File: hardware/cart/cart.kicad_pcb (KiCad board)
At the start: 2 copper layers, 40.1 x 26.2 mm, 3 parts, among them J1 Front Edge, J2 Back Edge, U1 Pro Micro

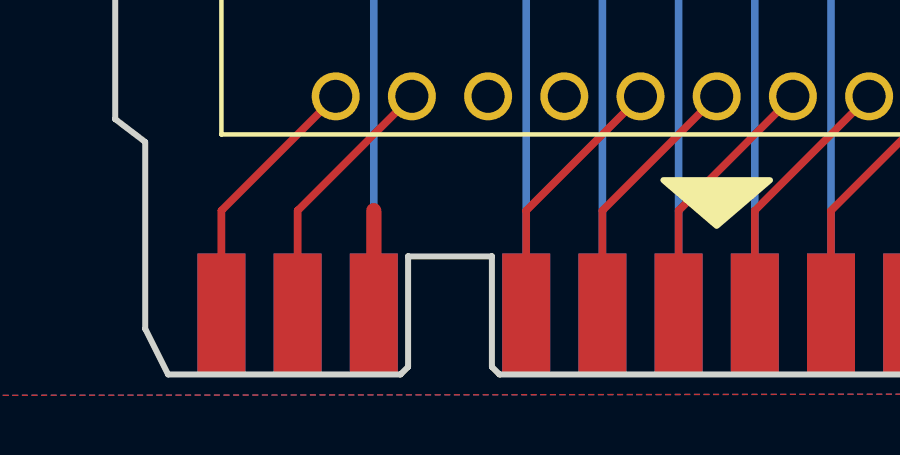
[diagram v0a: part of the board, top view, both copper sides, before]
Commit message: Add breakaway key pin filler
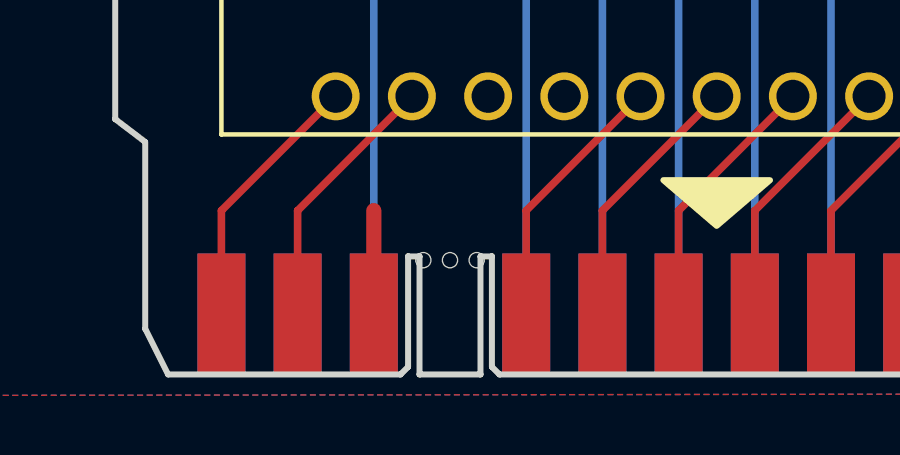
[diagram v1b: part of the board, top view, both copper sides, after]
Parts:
- added REF**: BREAKAWAY_HOLE, cart:BREAKAWAY_HOLE, F.Cu at (131.7, 124.8)
- added REF**: BREAKAWAY_HOLE, cart:BREAKAWAY_HOLE, F.Cu at (129.9, 124.8)
- added REF**: BREAKAWAY_HOLE, cart:BREAKAWAY_HOLE, F.Cu at (130.8, 124.8)
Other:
- outline, holes or cut-outs redrawn
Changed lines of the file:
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@@
   (general
     (thickness 1.6)
-    (drawings 41)
+    (drawings 45)
     (tracks 54)
     (zones 0)
-    (modules 3)
+    (modules 6)
     (nets 23)
   )
   (page USLetter)
   (layers
-    (0 F.Cu signal hide)
+    (0 F.Cu signal)
     (31 B.Cu signal hide)
     (32 B.Adhes user hide)
@@
     (36 B.SilkS user)
     (37 F.SilkS user)
-    (38 B.Mask user)
+    (38 B.Mask user hide)
     (39 F.Mask user hide)
     (40 Dwgs.User user hide)
@@
     (45 Margin user hide)
     (46 B.CrtYd user)
-    (47 F.CrtYd user hide)
+    (47 F.CrtYd user)
     (48 B.Fab user)
     (49 F.Fab user hide)
@@
     (mod_text_size 1 1)
     (mod_text_width 0.15)
-    (pad_size 5.15 5.15)
-    (pad_drill 0)
+    (pad_size 0.508 0.508)
+    (pad_drill 0.508)
     (pad_to_mask_clearance 0.0508)
     (solder_mask_min_width 0.25)
@@
     (add_net "Net-(J2-Pad8)")
     (add_net "Net-(J2-Pad9)")
+  )
+  (module cart:BREAKAWAY_HOLE (layer F.Cu)
+    (at 131.699 124.841)
+    (fp_text reference REF** (at 0 2.54) (layer F.SilkS) hide
+      (effects (font (size 1 1) (thickness 0.15)))
+    )
+    (fp_text value BREAKAWAY_HOLE (at 0 -2.54) (layer F.Fab)
+      (effects (font (size 1 1) (thickness 0.15)))
+    )
+    (pad "" np_thru_hole circle (at 0 0) (size 0.508 0.508) (drill 0.508) (layers *.Cu *.Mask))
+  )
+  (module cart:BREAKAWAY_HOLE (layer F.Cu)
+    (at 129.921 124.841)
+    (fp_text reference REF** (at 0 2.54) (layer F.SilkS) hide
+      (effects (font (size 1 1) (thickness 0.15)))
+    )
+    (fp_text value BREAKAWAY_HOLE (at 0 -2.54) (layer F.Fab)
+      (effects (font (size 1 1) (thickness 0.15)))
+    )
+    (pad "" np_thru_hole circle (at 0 0) (size 0.508 0.508) (drill 0.508) (layers *.Cu *.Mask))
+  )
+  (module cart:BREAKAWAY_HOLE (layer F.Cu)
+    (at 130.81 124.841)
+    (fp_text reference REF** (at 0 2.54) (layer F.SilkS) hide
+      (effects (font (size 1 1) (thickness 0.15)))
+    )
+    (fp_text value BREAKAWAY_HOLE (at 0 -2.54) (layer F.Fab)
+      (effects (font (size 1 1) (thickness 0.15)))
+    )
+    (pad "" np_thru_hole circle (at 0 0) (size 0.508 0.508) (drill 0.508) (layers *.Cu *.Mask))
   )
   (module cart:CARD_CONNECTOR_14_POS (layer B.Cu)
@@
       (net 3 "Net-(J1-Pad1)"))
   )
+  (gr_line (start 131.826 124.714) (end 132.207 124.714) (layer Edge.Cuts) (width 0.2))
+  (gr_line (start 129.794 128.651) (end 131.826 128.651) (layer Edge.Cuts) (width 0.2))
+  (gr_line (start 131.826 124.714) (end 131.826 128.651) (layer Edge.Cuts) (width 0.2))
+  (gr_line (start 129.794 124.714) (end 129.794 128.651) (layer Edge.Cuts) (width 0.2))
   (gr_text github.com/menehune23/arduboy-ce (at 139.7 122.301) (layer B.SilkS)
     (effects (font (size 0.762 0.762) (thickness 0.127)) (justify mirror))
@@
   (gr_line (start 132.461 128.651) (end 132.207 128.397) (layer Edge.Cuts) (width 0.2))
   (gr_line (start 129.413 128.397) (end 129.159 128.651) (layer Edge.Cuts) (width 0.2))
-  (gr_line (start 129.413 124.714) (end 132.207 124.714) (layer Edge.Cuts) (width 0.2))
+  (gr_line (start 129.413 124.714) (end 129.794 124.714) (layer Edge.Cuts) (width 0.2))
   (gr_line (start 132.207 124.714) (end 132.207 128.397) (layer Edge.Cuts) (width 0.2))
   (gr_line (start 129.413 124.714) (end 129.413 128.397) (layer Edge.Cuts) (width 0.2))

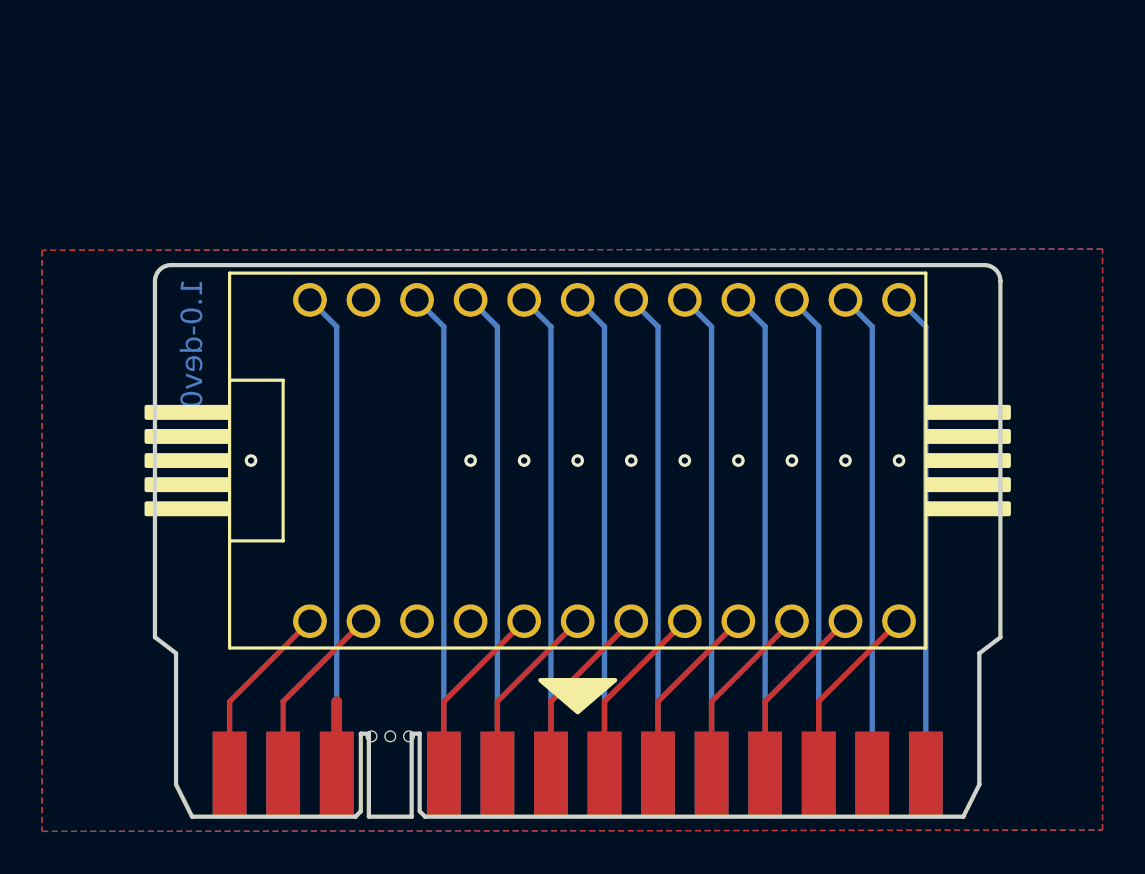
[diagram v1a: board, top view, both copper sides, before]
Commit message: System front/back, extend cart height
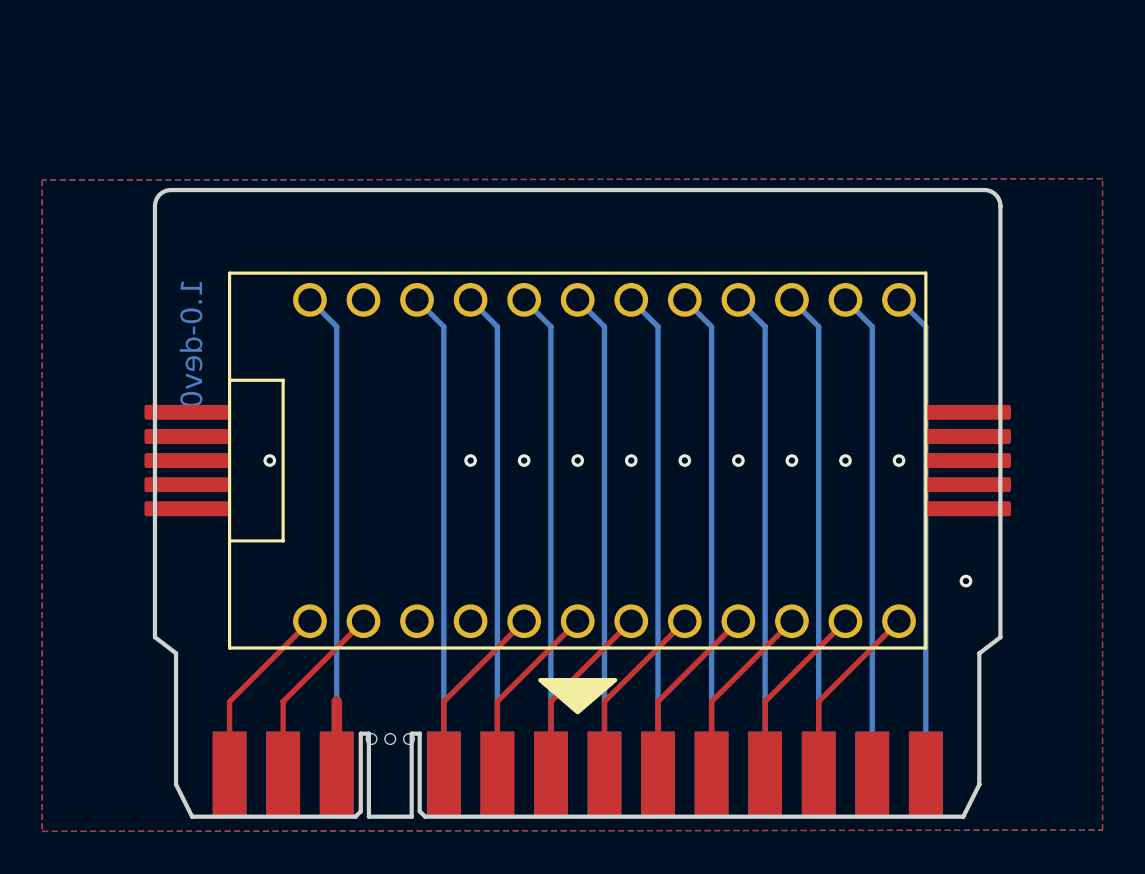
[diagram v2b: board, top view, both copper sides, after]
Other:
- board size 40.1 x 26.2 mm -> 40.1 x 29.7 mm
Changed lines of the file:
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@@
-(kicad_pcb (version 20171130) (host pcbnew "(5.1.2-1)-1")
+(kicad_pcb (version 20171130) (host pcbnew "(5.1.9-0-10_14)")
   (general
     (thickness 1.6)
-    (drawings 45)
+    (drawings 55)
     (tracks 54)
     (zones 0)
@@
   (layers
     (0 F.Cu signal)
-    (31 B.Cu signal hide)
+    (31 B.Cu signal)
     (32 B.Adhes user hide)
     (33 F.Adhes user hide)
@@
     (37 F.SilkS user)
     (38 B.Mask user hide)
-    (39 F.Mask user hide)
+    (39 F.Mask user)
     (40 Dwgs.User user hide)
     (41 Cmts.User user hide)
@@
       (effects (font (size 1 1) (thickness 0.15)))
     )
-    (pad "" np_thru_hole circle (at 0 0) (size 0.508 0.508) (drill 0.508) (layers *.Cu *.Mask))
+    (pad "" np_thru_hole circle (at 0 0.127) (size 0.508 0.508) (drill 0.508) (layers *.Cu *.Mask))
   )
   (module cart:BREAKAWAY_HOLE (layer F.Cu)
@@
       (effects (font (size 1 1) (thickness 0.15)))
     )
-    (pad "" np_thru_hole circle (at 0 0) (size 0.508 0.508) (drill 0.508) (layers *.Cu *.Mask))
+    (pad "" np_thru_hole circle (at 0 0.127) (size 0.508 0.508) (drill 0.508) (layers *.Cu *.Mask))
   )
   (module cart:BREAKAWAY_HOLE (layer F.Cu)
@@
       (effects (font (size 1 1) (thickness 0.15)))
     )
-    (pad "" np_thru_hole circle (at 0 0) (size 0.508 0.508) (drill 0.508) (layers *.Cu *.Mask))
+    (pad "" np_thru_hole circle (at 0 0.127) (size 0.508 0.508) (drill 0.508) (layers *.Cu *.Mask))
   )
   (module cart:CARD_CONNECTOR_14_POS (layer B.Cu)
@@
       (net 3 "Net-(J1-Pad1)"))
   )
+  (gr_poly (pts (xy 119.253 113.792) (xy 123.1265 113.792) (xy 123.1265 114.3) (xy 119.253 114.3)) (layer F.Cu) (width 0.2))
+  (gr_poly (pts (xy 119.253 112.649) (xy 123.1265 112.649) (xy 123.1265 113.157) (xy 119.253 113.157)) (layer F.Cu) (width 0.2))
+  (gr_poly (pts (xy 119.253 111.506) (xy 123.1265 111.506) (xy 123.1265 112.014) (xy 119.253 112.014)) (layer F.Cu) (width 0.2))
+  (gr_poly (pts (xy 119.253 110.363) (xy 123.1265 110.363) (xy 123.1265 110.871) (xy 119.253 110.871)) (layer F.Cu) (width 0.2))
+  (gr_poly (pts (xy 119.253 109.22) (xy 123.1265 109.22) (xy 123.1265 109.728) (xy 119.253 109.728)) (layer F.Cu) (width 0.2))
+  (gr_poly (pts (xy 156.2735 113.792) (xy 160.147 113.792) (xy 160.147 114.3) (xy 156.2735 114.3)) (layer F.Mask) (width 0.2))
+  (gr_poly (pts (xy 156.2735 112.649) (xy 160.147 112.649) (xy 160.147 113.157) (xy 156.2735 113.157)) (layer F.Mask) (width 0.2))
+  (gr_poly (pts (xy 156.2735 111.506) (xy 160.147 111.506) (xy 160.147 112.014) (xy 156.2735 112.014)) (layer F.Mask) (width 0.2))
+  (gr_poly (pts (xy 156.2735 110.363) (xy 160.147 110.363) (xy 160.147 110.871) (xy 156.2735 110.871)) (layer F.Mask) (width 0.2))
+  (gr_poly (pts (xy 156.2735 109.22) (xy 160.147 109.22) (xy 160.147 109.728) (xy 156.2735 109.728)) (layer F.Mask) (width 0.2))
   (gr_line (start 131.826 124.714) (end 132.207 124.714) (layer Edge.Cuts) (width 0.2))
   (gr_line (start 129.794 128.651) (end 131.826 128.651) (layer Edge.Cuts) (width 0.2))
@@
   (gr_line (start 129.413 124.714) (end 129.413 128.397) (layer Edge.Cuts) (width 0.2))
   (gr_line (start 157.988 128.651) (end 132.461 128.651) (layer Edge.Cuts) (width 0.2))
-  (gr_poly (pts (xy 119.253 113.792) (xy 123.1265 113.792) (xy 123.1265 114.3) (xy 119.253 114.3)) (layer F.SilkS) (width 0.2))
-  (gr_poly (pts (xy 119.253 110.363) (xy 123.1265 110.363) (xy 123.1265 110.871) (xy 119.253 110.871)) (layer F.SilkS) (width 0.2))
-  (gr_poly (pts (xy 119.253 112.649) (xy 123.1265 112.649) (xy 123.1265 113.157) (xy 119.253 113.157)) (layer F.SilkS) (width 0.2))
-  (gr_poly (pts (xy 119.253 111.506) (xy 123.1265 111.506) (xy 123.1265 112.014) (xy 119.253 112.014)) (layer F.SilkS) (width 0.2))
-  (gr_poly (pts (xy 119.253 109.22) (xy 123.1265 109.22) (xy 123.1265 109.728) (xy 119.253 109.728)) (layer F.SilkS) (width 0.2))
-  (gr_poly (pts (xy 156.2735 113.792) (xy 160.147 113.792) (xy 160.147 114.3) (xy 156.2735 114.3)) (layer F.SilkS) (width 0.2))
-  (gr_poly (pts (xy 156.2735 112.649) (xy 160.147 112.649) (xy 160.147 113.157) (xy 156.2735 113.157)) (layer F.SilkS) (width 0.2))
-  (gr_poly (pts (xy 156.2735 109.22) (xy 160.147 109.22) (xy 160.147 109.728) (xy 156.2735 109.728)) (layer F.SilkS) (width 0.2))
-  (gr_poly (pts (xy 156.2735 110.363) (xy 160.147 110.363) (xy 160.147 110.871) (xy 156.2735 110.871)) (layer F.SilkS) (width 0.2))
-  (gr_line (start 119.65 103.251) (end 119.65 120.139) (layer Edge.Cuts) (width 0.2))
+  (gr_poly (pts (xy 119.253 113.792) (xy 123.1265 113.792) (xy 123.1265 114.3) (xy 119.253 114.3)) (layer F.Mask) (width 0.2))
+  (gr_poly (pts (xy 119.253 110.363) (xy 123.1265 110.363) (xy 123.1265 110.871) (xy 119.253 110.871)) (layer F.Mask) (width 0.2))
+  (gr_poly (pts (xy 119.253 112.649) (xy 123.1265 112.649) (xy 123.1265 113.157) (xy 119.253 113.157)) (layer F.Mask) (width 0.2))
+  (gr_poly (pts (xy 119.253 111.506) (xy 123.1265 111.506) (xy 123.1265 112.014) (xy 119.253 112.014)) (layer F.Mask) (width 0.2))
+  (gr_poly (pts (xy 119.253 109.22) (xy 123.1265 109.22) (xy 123.1265 109.728) (xy 119.253 109.728)) (layer F.Mask) (width 0.2))
+  (gr_poly (pts (xy 156.2735 113.792) (xy 160.147 113.792) (xy 160.147 114.3) (xy 156.2735 114.3)) (layer F.Cu) (width 0.2))
+  (gr_poly (pts (xy 156.2735 112.649) (xy 160.147 112.649) (xy 160.147 113.157) (xy 156.2735 113.157)) (layer F.Cu) (width 0.2))
+  (gr_poly (pts (xy 156.2735 109.22) (xy 160.147 109.22) (xy 160.147 109.728) (xy 156.2735 109.728)) (layer F.Cu) (width 0.2))
+  (gr_poly (pts (xy 156.2735 110.363) (xy 160.147 110.363) (xy 160.147 110.871) (xy 156.2735 110.871)) (layer F.Cu) (width 0.2))
+  (gr_line (start 119.65 99.691) (end 119.65 120.139) (layer Edge.Cuts) (width 0.2))
   (gr_line (start 120.65 120.901) (end 119.65 120.139) (layer Edge.Cuts) (width 0.2))
-  (gr_arc (start 120.412 103.251) (end 120.412 102.489) (angle -90) (layer Edge.Cuts) (width 0.2))
+  (gr_arc (start 120.412 99.691) (end 120.412 98.929) (angle -90) (layer Edge.Cuts) (width 0.2))
   (gr_line (start 158.115 122.174) (end 158.115 105.283) (layer Dwgs.User) (width 0.15))
   (gr_line (start 159.75 120.142) (end 158.75 120.904) (layer Edge.Cuts) (width 0.2))
@@
   (gr_circle (center 174.625 93.98) (end 177.421885 93.98) (layer Cmts.User) (width 0.15))
   (gr_circle (center 174.625 88.265) (end 177.421885 88.265) (layer Cmts.User) (width 0.15))
-  (gr_poly (pts (xy 156.2735 111.506) (xy 160.147 111.506) (xy 160.147 112.014) (xy 156.2735 112.014)) (layer F.SilkS) (width 0.2))
-  (gr_line (start 159.75 103.251) (end 159.75 120.142) (layer Edge.Cuts) (width 0.2))
+  (gr_poly (pts (xy 156.2735 111.506) (xy 160.147 111.506) (xy 160.147 112.014) (xy 156.2735 112.014)) (layer F.Cu) (width 0.2))
+  (gr_line (start 159.75 99.691) (end 159.75 120.142) (layer Edge.Cuts) (width 0.2))
   (gr_poly (pts (xy 160.4645 124.6505) (xy 160.401 129.667) (xy 118.618 129.667) (xy 118.6815 124.6505)) (layer B.Mask) (width 0.1))
   (gr_poly (pts (xy 160.401 124.6505) (xy 160.401 129.667) (xy 118.618 129.667) (xy 118.618 124.6505)) (layer F.Mask) (width 0.1))
-  (gr_line (start 120.412 102.489) (end 158.988 102.489) (layer Edge.Cuts) (width 0.2))
-  (gr_arc (start 158.988 103.251) (end 159.75 103.251) (angle -90) (layer Edge.Cuts) (width 0.2))
+  (gr_line (start 120.412 98.929) (end 158.988 98.929) (layer Edge.Cuts) (width 0.2))
+  (gr_arc (start 158.988 99.691) (end 159.75 99.691) (angle -90) (layer Edge.Cuts) (width 0.2))
   (gr_text 1.0-dev0 (at 121.412 103.124 90) (layer B.Cu)
     (effects (font (size 1.016 1.016) (thickness 0.2286)) (justify left mirror))
@@
   (via (at 152.4 111.76) (size 0.6) (drill 0.3) (layers F.Cu B.Cu) (net 1))
   (via (at 154.94 111.76) (size 0.6) (drill 0.3) (layers F.Cu B.Cu) (net 1))
-  (via (at 158.115 111.76) (size 0.6) (drill 0.3) (layers F.Cu B.Cu) (net 1))
-  (via (at 124.206 111.76) (size 0.6) (drill 0.3) (layers F.Cu B.Cu) (net 1))
+  (via (at 158.115 117.475) (size 0.6) (drill 0.3) (layers F.Cu B.Cu) (net 1))
+  (via (at 125.095 111.76) (size 0.6) (drill 0.3) (layers F.Cu B.Cu) (net 1))
   (segment (start 125.73 123.19) (end 125.73 126.619) (width 0.254) (layer F.Cu) (net 2))
   (segment (start 129.54 119.38) (end 125.73 123.19) (width 0.254) (layer F.Cu) (net 2))
@@
     (polygon
       (pts
-        (xy 164.592 101.727) (xy 114.3 101.7905) (xy 114.3 129.3495) (xy 164.592 129.286)
+        (xy 164.592 98.39325) (xy 114.3 98.45675) (xy 114.3 129.3495) (xy 164.592 129.286)
       )
     )
@@
     (polygon
       (pts
-        (xy 164.592 101.727) (xy 114.3 101.7905) (xy 114.3 129.3495) (xy 164.592 129.286)
+        (xy 164.592 98.39325) (xy 114.3 98.45675) (xy 114.3 129.3495) (xy 164.592 129.286)
       )
     )

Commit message: Add JLC order number lables
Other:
- board text added: "JLCJLCJLCJLC"
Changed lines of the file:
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@@
   (general
     (thickness 1.6)
-    (drawings 55)
+    (drawings 56)
     (tracks 54)
     (zones 0)
@@
   (page USLetter)
   (layers
-    (0 F.Cu signal)
+    (0 F.Cu signal hide)
     (31 B.Cu signal)
     (32 B.Adhes user hide)
@@
     (35 F.Paste user hide)
     (36 B.SilkS user)
-    (37 F.SilkS user)
-    (38 B.Mask user hide)
-    (39 F.Mask user)
+    (37 F.SilkS user hide)
+    (38 B.Mask user)
+    (39 F.Mask user hide)
     (40 Dwgs.User user hide)
     (41 Cmts.User user hide)
@@
     (45 Margin user hide)
     (46 B.CrtYd user)
-    (47 F.CrtYd user)
+    (47 F.CrtYd user hide)
     (48 B.Fab user)
     (49 F.Fab user hide)
@@
       (effects (font (size 1 1) (thickness 0.15)))
     )
+    (fp_line (start -16.51 8.89) (end 16.51 8.89) (layer F.SilkS) (width 0.15))
+    (fp_line (start -16.51 8.89) (end -16.51 3.81) (layer F.SilkS) (width 0.15))
+    (fp_line (start -13.97 3.81) (end -16.51 3.81) (layer F.SilkS) (width 0.15))
+    (fp_line (start -16.51 3.81) (end -16.51 -3.81) (layer F.SilkS) (width 0.15))
+    (fp_line (start -16.51 -3.81) (end -13.97 -3.81) (layer F.SilkS) (width 0.15))
+    (fp_line (start -16.51 -3.81) (end -16.51 -8.89) (layer F.SilkS) (width 0.15))
+    (fp_line (start -16.51 -8.89) (end 16.51 -8.89) (layer F.SilkS) (width 0.15))
+    (fp_line (start 16.51 -8.89) (end 16.51 8.89) (layer F.SilkS) (width 0.15))
     (fp_line (start -13.97 3.81) (end -13.97 -3.81) (layer F.SilkS) (width 0.15))
-    (fp_line (start 16.51 -8.89) (end 16.51 8.89) (layer F.SilkS) (width 0.15))
-    (fp_line (start -16.51 -8.89) (end 16.51 -8.89) (layer F.SilkS) (width 0.15))
-    (fp_line (start -16.51 -3.81) (end -16.51 -8.89) (layer F.SilkS) (width 0.15))
-    (fp_line (start -16.51 -3.81) (end -13.97 -3.81) (layer F.SilkS) (width 0.15))
-    (fp_line (start -16.51 3.81) (end -16.51 -3.81) (layer F.SilkS) (width 0.15))
-    (fp_line (start -13.97 3.81) (end -16.51 3.81) (layer F.SilkS) (width 0.15))
-    (fp_line (start -16.51 8.89) (end -16.51 3.81) (layer F.SilkS) (width 0.15))
-    (fp_line (start -16.51 8.89) (end 16.51 8.89) (layer F.SilkS) (width 0.15))
     (pad 24 thru_hole circle (at -12.7 -7.62) (size 1.6 1.6) (drill 1.1) (layers *.Cu *.Mask F.SilkS)
       (net 12 "Net-(J2-Pad12)"))
@@
       (net 3 "Net-(J1-Pad1)"))
   )
+  (gr_text JLCJLCJLCJLC (at 123.444 103.378 90) (layer B.SilkS)
+    (effects (font (size 0.762 0.762) (thickness 0.127)) (justify left mirror))
+  )
   (gr_poly (pts (xy 119.253 113.792) (xy 123.1265 113.792) (xy 123.1265 114.3) (xy 119.253 114.3)) (layer F.Cu) (width 0.2))
